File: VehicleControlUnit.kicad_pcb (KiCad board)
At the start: 2 copper layers, 86.6 x 100 mm, 105 parts, among them Con1 LED, Con2 LED, J1 Conn_01x02, J10 USB_C_Receptacle_USB2.0_16P, J11 UART_Breakout, J12 Conn_01x04, J13 Conn_01x04, J14 Conn_01x04, J15 Conn_01x08, J16 Conn_01x08, J2 Precharge_Ready, J4 Conn_01x02, J5 Conn_01x02, J6 Conn_01x04, J7 Conn_01x04, J8 MOTOR_CAN_Breakout, J9 CAR_CAN_Breakout, Q1 PMV35EPER, Q2 IRLML0030, Q3 IRLML0030, SW1 RESET, SW2 BOOT, U1 TLV1117LV33DCYR, U3 ESP32-C6-MINI-1/U, U4 TCMT1106, U5 TCMT1106

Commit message: fuck the rats nest im doing it tomorrow
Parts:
- removed J12, J13: Conn_01x04, utsvt_conn:Molex_MicroFit3.0_1x4xP3.00mm_PolarizingPeg_Vertical
- removed J16: Conn_01x08, Connector_PinHeader_2.54mm:PinHeader_1x08_P2.54mm_Vertical
- removed R28, R29, R30: 1k, Resistor_SMD:R_0805_2012Metric
- added C18: 0.1u, Capacitor_SMD:C_0805_2012Metric, F.Cu at (95.3, 60.7)
- added U6: TCMT1106, Package_SO:SOP-4_4.4x2.6mm_P1.27mm, F.Cu at (97.9, 55.1)
- C1: value 1u -> 220n
- C10, C3: value 0.1u -> 10u
- C11: value 10u -> 0.1u
- C12: value 1u -> 10u
- C13, C15, C7: value 0.1u -> 1u
- C14, C4, C8: value 1u -> 0.1u
- C2: value 10u -> 22n
- C9: value 10u -> 1u
- D1: footprint Active-PrechargeLib:BZT52B12QX -> UTSVT_Passives:BZT52B12QX
- D5: footprint tv diode:PRTR5V0U2X -> UTSVT_Passives:PRTR5V0U2X
- D7, D8: footprint Active-PrechargeLib:SODFL4724X108N -> UTSVT_Passives:SODFL4724X108N
- J1: footprint utsvt_conn:Molex_MicroFit3.0_1x2xP3.00mm_PolarizingPeg_Vertical -> UTSVT_Connectors:Molex_MicroFit3.0_1x2xP3.00mm_PolarizingPeg_Vertical
- J10: value USB_C_Receptacle_USB2.0_16P -> Conn_01x04; footprint USBC:GCT_USB4215-03-A_REVA -> UTSVT_Connectors:Molex_MicroFit3.0_1x4xP3.00mm_PolarizingPeg_Vertical
- J11: value UART_Breakout -> Conn_01x04; footprint Connector_PinHeader_2.54mm:PinHeader_1x02_P2.54mm_Vertical -> UTSVT_Connectors:Molex_MicroFit3.0_1x4xP3.00mm_PolarizingPeg_Vertical
- J14: value Conn_01x04 -> SFH11-PBPC-D05-ST-BK; footprint Connector_PinHeader_2.54mm:PinHeader_1x04_P2.54mm_Vertical -> UTSVT_Connectors:CONN_SFH11-xxxC-D05-ST-XX_SUL
- J15: value Conn_01x08 -> SFH11-PBPC-D05-ST-BK; footprint Connector_PinHeader_2.54mm:PinHeader_1x08_P2.54mm_Vertical -> UTSVT_Connectors:CONN_SFH11-xxxC-D05-ST-XX_SUL
- J2: value Precharge_Ready -> Conn_01x02
- J3: value ~ -> Conn_01x02; footprint UTSVT_Special:LeaderSOM -> Connector_Molex:Molex_Nano-Fit_105309-xx02_1x02_P2.50mm_Vertical
- J4: value Conn_01x02 -> ~; footprint Connector_Molex:Molex_Nano-Fit_105309-xx02_1x02_P2.50mm_Vertical -> UTSVT_Special:LeaderSOM
- J5: value Conn_01x02 -> SFH11-PBPC-D05-ST-BK; footprint Connector_Molex:Molex_Nano-Fit_105309-xx02_1x02_P2.50mm_Vertical -> UTSVT_Connectors:CONN_SFH11-xxxC-D05-ST-XX_SUL
- J6: value Conn_01x04 -> SFH11-PBPC-D05-ST-BK; footprint Connector_Molex:Molex_Nano-Fit_105309-xx04_1x04_P2.50mm_Vertical -> UTSVT_Connectors:CONN_SFH11-xxxC-D05-ST-XX_SUL
- J8: value MOTOR_CAN_Breakout -> Conn_01x04; footprint Connector_PinHeader_2.54mm:PinHeader_1x02_P2.54mm_Vertical -> Connector_Molex:Molex_Nano-Fit_105309-xx04_1x04_P2.50mm_Vertical
- J9: value CAR_CAN_Breakout -> USB_C_Receptacle_USB2.0_16P; footprint Connector_PinHeader_2.54mm:PinHeader_1x02_P2.54mm_Vertical -> UTSVT_Connectors:GCT_USB4215-03-A_REVA
- Q1: value PMV35EPER -> PSMN8R5-40MSDX; footprint Package_TO_SOT_SMD:SOT-23-3 -> UTSVT_Power:BUK7M1780EX
- R1: value 49.9k -> 4k
- R10: value 1k -> 5.1k
- R11: value 10k -> 5.1k
- R12, R8: value 1k -> 10k
- R13: value 5.1k -> 100
- R14: value 5.1k -> 1k
- R16, R21: value 100 -> 4k
- R17, R22: value 4k -> 10k
- R18: value 10k -> 100
- R19, R24, R4: value 4k -> 1k
- R2: value 100 -> 1k
- R25, R26, R3: value 10k -> 1k
- U1: value TLV1117LV33DCYR -> LM74501-Q1; footprint Package_TO_SOT_SMD:SOT-223-3_TabPin2 -> Package_TO_SOT_SMD:SOT-23-8
- U2: value ~ -> TLV1117LV33DCYR; footprint LM66200:SOTFL50P160X60-8N -> Package_TO_SOT_SMD:SOT-223-3_TabPin2
- U3: value ESP32-C6-MINI-1/U -> ~; footprint ESP32-C6-MINI-1:ESP32-C6-MINI-1 -> UTSVT_Power:SOTFL50P160X60-8N
- U4: value TCMT1106 -> ESP32-C6-MINI-1/U; footprint Package_SO:SOP-4_4.4x2.6mm_P1.27mm -> UTSVT_Special:ESP32-C6-MINI-1
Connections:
- C1 pad 1: /Precharge_Ready -> Net-(U1-VCap)
- C1 pad 2: GND -> /LV+
- C11 pad 1: /ESP/5V_USB -> /ESP/3V3
- C12 pad 1: GND -> /ESP/5V_USB
- C12 pad 2: /M_Sense -> GND
- C13 pad 1: Net-(J12-Pin_2) -> GND
- C13 pad 2: GND -> /M_Sense
- C14 pad 1: GND -> Net-(J10-Pin_2)
- C14 pad 2: /MPre_Sense -> GND
- C15 pad 1: Net-(J13-Pin_2) -> GND
- C15 pad 2: GND -> /MPre_Sense
- C16 pad 1: /ESP/RESET -> Net-(J11-Pin_2)
- C17 pad 1: /ESP/BOOT -> /ESP/RESET
- C2 pad 1: +24V -> Net-(Q1-G)
- C2 pad 2: GND -> /LV+
- C4 pad 1: 3V3_LSOM -> +24V
- C5 pad 1: /ESP/5V_USB -> 3V3_LSOM
- C6 pad 1: /ESP/3V3_USB -> /ESP/5V_USB
- C7 pad 1: /ESP/3V3 -> /ESP/3V3_USB
- C8 pad 1: /ESP/3V3_USB -> /ESP/3V3
- C9 pad 1: /ESP/3V3 -> /ESP/3V3_USB
- D1 pad 2: Net-(D1-A) -> GND
- J11 pad 1: /ESP_TX -> +24V
- J11 pad 2: /ESP_RX -> Net-(J11-Pin_2)
- J15 pad 1: /ESP/IO5 -> /ESP/IO10
- J15 pad 2: /ESP/IO6 -> /ESP/IO11
- J15 pad 3: /ESP/IO7 -> /ESP/IO12
- J15 pad 4: /ESP/IO8 -> /ESP/IO13
- J15 pad 5: /ESP/IO9 -> /ESP/USB_D+
- J15 pad 6: /ESP/IO10 -> /ESP/USB_D-
- J15 pad 7: /ESP/IO11 -> unconnected-(J15-Pad7)
- J15 pad 8: /ESP/IO12 -> unconnected-(J15-Pad8)
- J2 pad 1: 3V3_LSOM -> GND
- J2 pad 2: Net-(J2-Pin_2) -> /VPrecharge+
- J3 pad 1: 3V3_LSOM -> GND
- J3 pad 2: 3V3_LSOM -> /VPrecharge-
- J4 pad 1: GND -> 3V3_LSOM
- J4 pad 2: /VPrecharge+ -> 3V3_LSOM
- J5 pad 1: GND -> /M_Enable
- J5 pad 2: /VPrecharge- -> /MPre_Enable
- J6 pad 1: /C_CAN_L -> /M_CAN_H
- J6 pad 2: /C_CAN_H -> /M_CAN_L
- J6 pad 3: /C_CAN_L -> /C_CAN_H
- J6 pad 4: /C_CAN_H -> /C_CAN_L
- J7 pad 1: /M_CAN_L -> /C_CAN_L
- J7 pad 2: /M_CAN_H -> /C_CAN_H
- J8 pad 1: /M_CAN_H -> /M_CAN_L
- J8 pad 2: /M_CAN_L -> /M_CAN_H
- Q1 pad 1: Net-(D1-A) -> /LV+
- Q1 pad 2: +24V -> /LV+
- R1 pad 1: GND -> +24V
- R1 pad 2: Net-(D1-A) -> Net-(LVPWR1-A)
- R10 pad 1: /ESP/3V3_USB -> /ESP/CC1
- R10 pad 2: Net-(D3-A) -> GND
- R11 pad 1: Net-(U2-!ON) -> /ESP/CC2
- R12 pad 1: 3V3_LSOM -> /M_Sense
- R12 pad 2: Net-(U2-ST) -> GND
- R13 pad 1: /ESP/CC1 -> /M_Sense
- R13 pad 2: GND -> Net-(R13-Pad2)
- R14 pad 1: /ESP/CC2 -> Net-(J10-Pin_2)
- R14 pad 2: GND -> Net-(R14-Pad2)
- R15 pad 1: /M_Sense -> /M_Enable
- R16 pad 1: /M_Sense -> Net-(Con1-A)
- R16 pad 2: Net-(R16-Pad2) -> +24V
- R17 pad 1: Net-(J12-Pin_2) -> /MPre_Sense
- R17 pad 2: Net-(R17-Pad2) -> GND
- R18 pad 1: /M_Enable -> /MPre_Sense
- R18 pad 2: GND -> Net-(R18-Pad2)
- R19 pad 1: Net-(Con1-A) -> Net-(J11-Pin_2)
- R19 pad 2: +24V -> Net-(R19-Pad2)
- R2 pad 1: Net-(J2-Pin_2) -> /LED1
- R2 pad 2: /Precharge_Ready -> Net-(LED1-A)
- R20 pad 1: /MPre_Sense -> /MPre_Enable
- R21 pad 1: /MPre_Sense -> Net-(Con2-A)
- R21 pad 2: Net-(R21-Pad2) -> +24V
- R22 pad 1: Net-(J13-Pin_2) -> /ESP/Buttons_LEDs_IO/3V3
- R22 pad 2: Net-(R22-Pad2) -> /ESP/RESET
- R23 pad 1: /MPre_Enable -> /ESP/Buttons_LEDs_IO/3V3
- R23 pad 2: GND -> /ESP/BOOT
- R24 pad 1: Net-(Con2-A) -> /ESP/LED1
- R24 pad 2: +24V -> Net-(LV1-A)
- R25 pad 1: /ESP/Buttons_LEDs_IO/3V3 -> /ESP/LED2
- R25 pad 2: /ESP/RESET -> Net-(LV2-A)
- R26 pad 1: /ESP/Buttons_LEDs_IO/3V3 -> /ESP/LED3
- R26 pad 2: /ESP/BOOT -> Net-(LV3-A)
- R27 pad 1: /ESP/LED1 -> /ESP/LED4
- R27 pad 2: Net-(LV1-A) -> Net-(LV4-A)
- R3 pad 1: /Precharge_Ready -> /LED2
- R3 pad 2: GND -> Net-(LED2-A)
- R4 pad 1: +24V -> /LED3
- R4 pad 2: Net-(LVPWR1-A) -> Net-(LED3-A)
- R5 pad 1: /LED1 -> /LED4
- R5 pad 2: Net-(LED1-A) -> Net-(LED4-A)
- R6 pad 1: /LED2 -> /ESP/5V_USB
- R6 pad 2: Net-(LED2-A) -> Net-(D2-A)
- R7 pad 1: /LED3 -> /ESP/3V3_USB
- R7 pad 2: Net-(LED3-A) -> Net-(D3-A)
- R8 pad 1: /LED4 -> Net-(U3-!ON)
- R8 pad 2: Net-(LED4-A) -> GND
- R9 pad 1: /ESP/5V_USB -> 3V3_LSOM
- R9 pad 2: Net-(D2-A) -> Net-(U3-ST)
- SW1 pad 2: /ESP/RESET -> GND
- SW2 pad 2: /ESP/BOOT -> GND
- U1 pad 1: GND -> Net-(Q1-G)
- U1 pad 2: /ESP/3V3_USB -> /LV+
- U1 pad 3: /ESP/5V_USB -> Net-(U1-VCap)
- U2 pad 2: /ESP/3V3 -> /ESP/3V3_USB
- U2 pad 3: 3V3_LSOM -> /ESP/5V_USB
- U3 pad 2: GND -> /ESP/3V3
- U3 pad 3: /ESP/3V3 -> 3V3_LSOM
- U3 pad 4: unconnected-(U3-NC-Pad4) -> Net-(U3-!ON)
- U3 pad 5: /ESP/IO12 -> GND
- U3 pad 6: /ESP/IO11 -> /ESP/3V3_USB
- U3 pad 7: unconnected-(U3-NC-Pad7) -> /ESP/3V3
- U3 pad 8: /ESP/RESET -> Net-(U3-ST)
- U4 pad 1: Net-(R17-Pad2) -> GND
- U4 pad 3: Net-(R16-Pad2) -> /ESP/3V3
- U4 pad 4: 3V3_LSOM -> unconnected-(U4-NC-Pad4)
- U5 pad 1: Net-(R22-Pad2) -> Net-(R14-Pad2)
- U5 pad 3: Net-(R21-Pad2) -> Net-(R13-Pad2)
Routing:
- net +24V: track 0.00 -> 87.4 mm, vias 39 -> 40
- net /ESP_TX: track 80.2 -> 0.00 mm, vias 1 -> 0
- net /VPrecharge-: track 76.8 -> 0.00 mm, vias 1 -> 0
- net /MPre_Enable: track 88.4 -> 165.3 mm, vias 3 -> 4
- net /LED2: track 51.9 -> 0.00 mm, vias 2 -> 0
- net /ESP/5V_USB: track 12.0 -> 64.0 mm, vias 0 -> 2
- net Net-(U3-!ON): track 0.00 -> 51.6 mm, vias 0 -> 2
- net /LED3: track 49.8 -> 0.00 mm, vias 2 -> 0
- net /ESP/3V3_USB: track 20.3 -> 70.1 mm, vias 0 -> 2
- net /LED1: track 49.4 -> 0.00 mm, vias 2 -> 0
- net /ESP/LED1: track 40.1 -> 0.00 mm, vias 2 -> 0
- net /ESP/LED4: track 37.7 -> 77.7 mm, vias 2 -> 4
- net /ESP_RX: track 78.0 -> 47.4 mm, vias 1 -> 0
- net Net-(J11-Pin_2): track 0.00 -> 30.7 mm, vias 0 -> 1
- net (no net): track 0.00 -> 24.4 mm
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
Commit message: routing done
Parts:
- removed M_Pre_Sen_TP1, M_Sen_TP1: TestPoint, UTSVT_Special:TestPoint_HEX_3mmID
- added C19: 0.1u, Capacitor_SMD:C_0805_2012Metric, F.Cu at (136.0, 51.5)
- added G***: LHRs_LOGO, UTSVT_Logos:LHRs_LOGO, F.Cu at (120.0, 96.8)
- G***: moved to B.Cu
- J2, J3: footprint Connector_Molex:Molex_Nano-Fit_105309-xx02_1x02_P2.50mm_Vertical -> UTSVT_Connectors:Molex_Nano-Fit_105309-xx02_1x02_P2.50mm_Vertical
- J7, J8: footprint Connector_Molex:Molex_Nano-Fit_105309-xx04_1x04_P2.50mm_Vertical -> UTSVT_Connectors:Molex_Nano-Fit_105309-xx04_1x04_P2.50mm_Vertical
- J9: footprint UTSVT_Connectors:GCT_USB4215-03-A_REVA -> UTSVT_Connectors:USB_C_Receptacle_GCT_USB4105-xx-A_16P_TopMnt_Horizontal
- moved J9 91.9 mm to (113.0, 125.2), turned to -90 degrees
- moved U4 81.6 mm to (125.6, 138.1), turned to 180 degrees
- moved G*** 74.1 mm to (140.0, 55.0), turned to 180 degrees
- moved J2 73.8 mm to (165.8, 45.3), turned to 90 degrees
- moved R7 69.0 mm to (130.8, 124.3), turned to 0 degrees
- moved J4 68.6 mm to (150.9, 112.3)
- moved R14 67.3 mm to (119.3, 63.0), turned to 0 degrees
- moved J3 67.0 mm to (156.2, 45.4)
- moved C18 66.0 mm to (160.8, 68.7), turned to 180 degrees
- moved U1 63.7 mm to (139.3, 55.5)
- moved R6 61.8 mm to (128.4, 113.0), turned to 180 degrees
- moved C4 61.7 mm to (150.6, 48.8), turned to 90 degrees
- moved J11 60.8 mm to (114.0, 86.0), turned to 90 degrees
- moved C12 58.5 mm to (124.8, 119.0)
- moved R2 58.4 mm to (176.2, 76.8), turned to 90 degrees
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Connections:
- J14 pad 1: /ESP/IO1 -> /ESP/IO4
- J14 pad 2: /ESP/IO2 -> /ESP/IO13
- J14 pad 4: /ESP/IO4 -> unconnected-(J14-Pad4)
- J14 pad 5: /ESP/IO5 -> /ESP/IO2
- J14 pad 6: /ESP/IO6 -> unconnected-(J14-Pad6)
- J14 pad 7: /ESP/IO7 -> /ESP/IO1
- J14 pad 8: /ESP/IO8 -> unconnected-(J14-Pad8)
- J14 pad 9: /ESP/IO9 -> GND
- J15 pad 1: /ESP/IO10 -> /ESP/IO11
- J15 pad 2: /ESP/IO11 -> /ESP/IO12
- J15 pad 3: /ESP/IO12 -> /ESP/IO9
- J15 pad 4: /ESP/IO13 -> /ESP/IO10
- J15 pad 5: /ESP/USB_D+ -> /ESP/IO7
- J15 pad 6: /ESP/USB_D- -> /ESP/IO8
- J15 pad 7: unconnected-(J15-Pad7) -> /ESP/IO5
- J15 pad 8: unconnected-(J15-Pad8) -> /ESP/IO6
- J15 pad 9: unconnected-(J15-Pad9) -> GND
- J5 pad 1: /M_Enable -> 3V3_LSOM
- J5 pad 2: /MPre_Enable -> /M_Enable
- J5 pad 3: /M_Sense -> /MPre_Enable
- J5 pad 4: /MPre_Sense -> /VPrecharge-
- J5 pad 7: /VPrecharge- -> /M_Sense
- J5 pad 8: /Precharge_Ready -> /MPre_Sense
- J5 pad 9: unconnected-(J5-Pad9) -> GND
- J6 pad 5: /ESP_RX -> /ESP_TX
- J6 pad 6: /ESP_TX -> /ESP_RX
- J6 pad 9: unconnected-(J6-Pad9) -> GND
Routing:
- net /ESP_TX: track 0.00 -> 130.6 mm, vias 0 -> 3
- net /MPre_Enable: track 165.3 -> 63.0 mm
- net +24V: track 87.4 -> 3.36 mm, vias 40 -> 46
- net /ESP_RX: track 47.4 -> 131.0 mm, vias 0 -> 5
- net /Precharge_Ready: track 78.5 -> 0.00 mm, vias 2 -> 0
- net /VPrecharge-: track 0.00 -> 74.6 mm, vias 0 -> 2
- net /LED2: track 0.00 -> 51.9 mm, vias 0 -> 2
- net /ESP/5V_USB: track 64.0 -> 12.6 mm, vias 2 -> 0
- net /LED3: track 0.00 -> 49.8 mm, vias 0 -> 2
- net /ESP/3V3_USB: track 70.1 -> 20.4 mm, vias 2 -> 0
- net /LED1: track 0.00 -> 49.4 mm, vias 0 -> 2
- net Net-(U3-!ON): track 51.6 -> 3.07 mm, vias 2 -> 0
- net 3V3_LSOM: track 153.8 -> 105.7 mm, vias 8 -> 4
- net /ESP/LED1: track 0.00 -> 40.1 mm, vias 0 -> 2
- net /ESP/LED4: track 77.7 -> 37.7 mm, vias 4 -> 2
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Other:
- outline, holes or cut-outs redrawn
- board text added: "24V"
- board text added: "BPS"
- board text added: "Boot"
- board text added: "GND"
- board text added: "Precharge"
- board text added: "Reset"
- board text added: "Sense"
- board text added: "Timeout"
- board text removed: "C_CAN_H C_CAN_L"
- board text removed: "ESP LEDS"
- board text removed: "LSOM LEDS"
- board text removed: "MPre_Sense"
- board text removed: "M_CAN_H M_CAN_L"
- board text removed: "M_Sense"
- board text removed: "TX RX"
- board text removed: "UART_BREAKOUT"

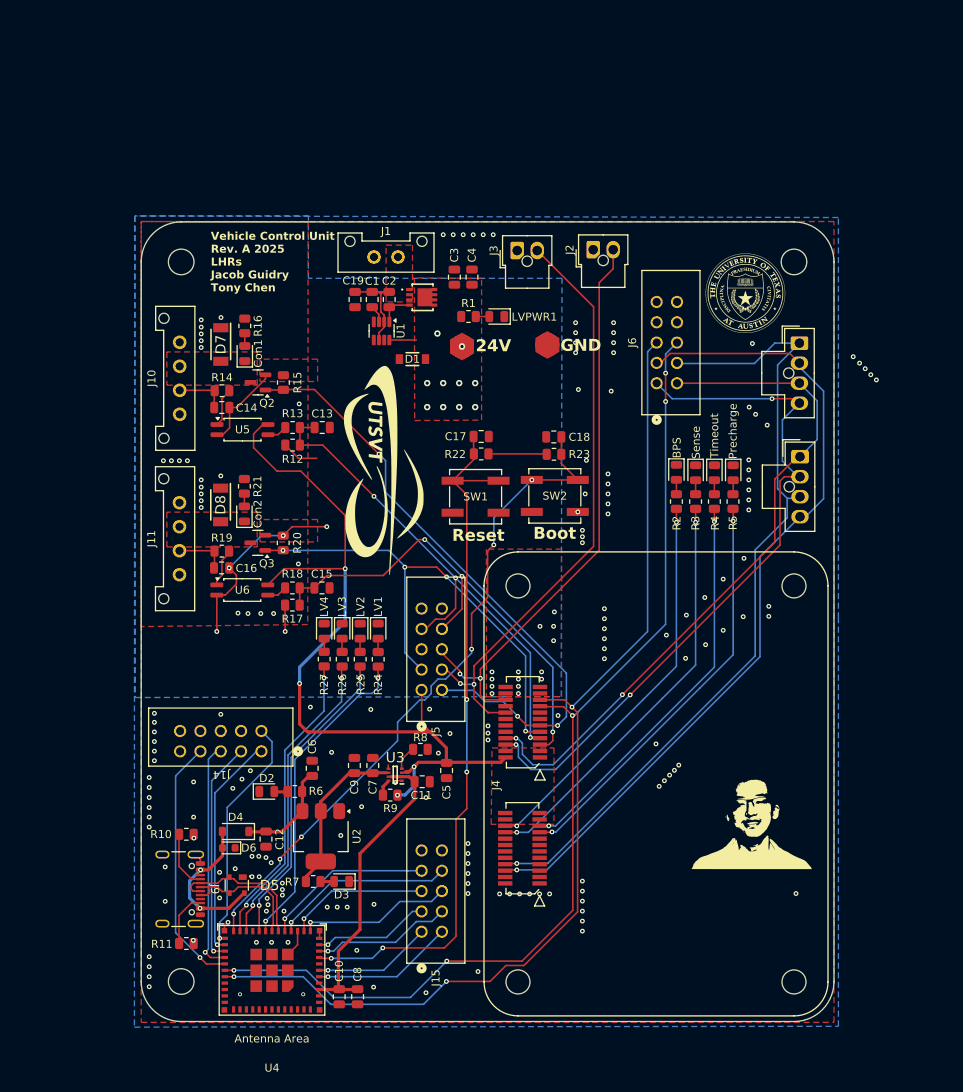
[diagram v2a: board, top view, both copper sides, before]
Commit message: replace microfit with nanofit and some layout adjustments
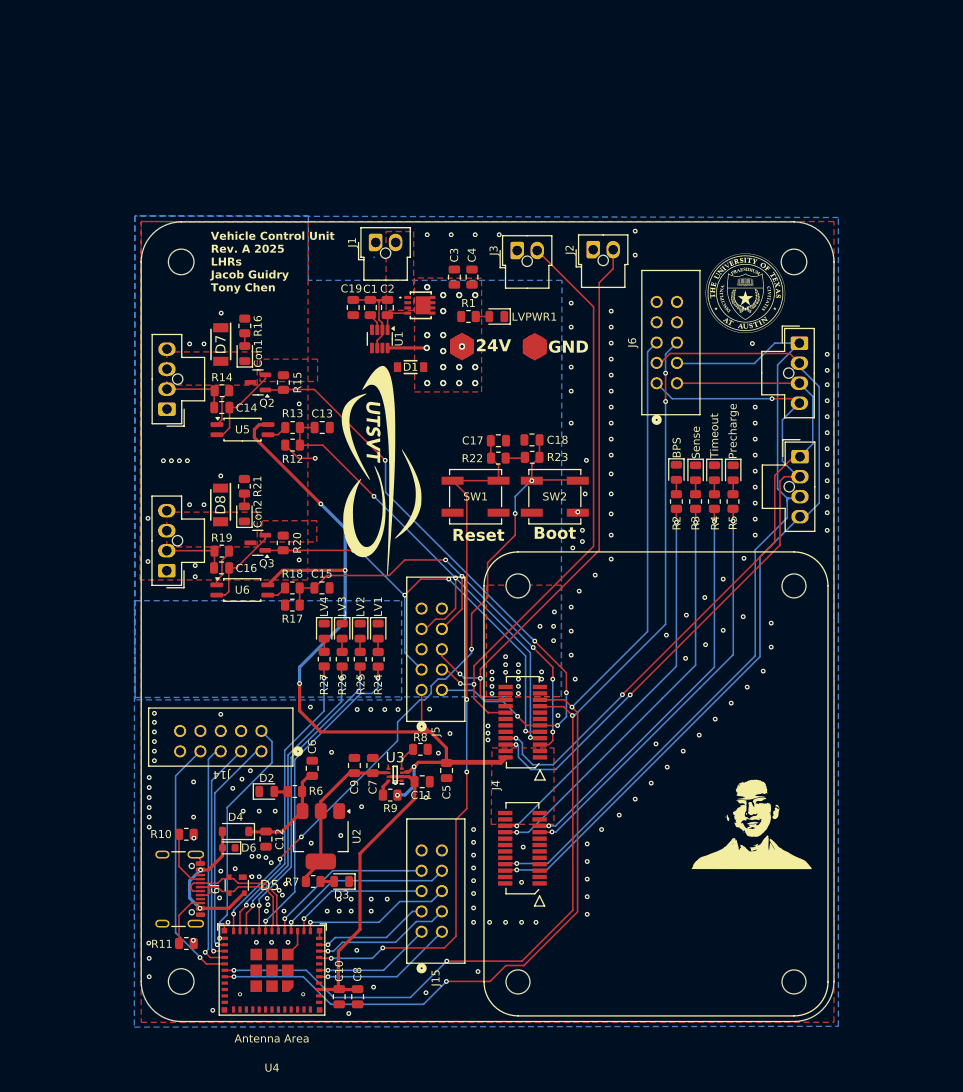
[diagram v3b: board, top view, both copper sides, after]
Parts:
- added G***: LOGO, UTSVT_Logos:Hallock_Image_Tiny, B.Cu at (185.6, 117.2)
- J1: footprint UTSVT_Connectors:Molex_MicroFit3.0_1x2xP3.00mm_PolarizingPeg_Vertical -> UTSVT_Connectors:Molex_Nano-Fit_105309-xx02_1x02_P2.50mm_Vertical
- J10, J11: footprint UTSVT_Connectors:Molex_MicroFit3.0_1x4xP3.00mm_PolarizingPeg_Vertical -> UTSVT_Connectors:Molex_Nano-Fit_105309-xx04_1x04_P2.50mm_Vertical
- moved J10 3.95 mm to (112.7, 62.2), turned to 180 degrees
- moved J11 3.81 mm to (112.7, 82.4), turned to 180 degrees
- moved C18 2.75 mm to (158.1, 69.1)
- moved R23 2.75 mm to (158.1, 71.3)
- moved C17 2.21 mm to (153.9, 69.2)
- moved R22 2.21 mm to (153.9, 71.4)
- moved J1 1.83 mm to (138.6, 44.4), turned to 90 degrees
- moved LVGND_TP1 1.59 mm to (158.4, 57.5)
- moved Q1 1.03 mm to (144.2, 52.3)
- moved U1 1.03 mm to (139.1, 56.5)
- moved C1 1.02 mm to (137.9, 52.5)
- moved C19 1.02 mm to (135.8, 52.5)
- moved C2 1.02 mm to (140.0, 52.5)
- moved D1 1.02 mm to (142.9, 60.0)
- moved G*** 0.27 mm to (139.2, 73.1)
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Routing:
- net GND: track 52.1 -> 35.7 mm, vias 159 -> 183
- net /ESP/Buttons_LEDs_IO/3V3: track 7.30 -> 2.44 mm
- net 3V3_LSOM: track 105.7 -> 103.1 mm, vias 4 -> 5
- net /LV+: track 12.4 -> 10.1 mm
- net /MPre_Sense: track 61.5 -> 59.4 mm, vias 3 -> 5
- net /MPre_Enable: track 63.0 -> 61.1 mm
- net Net-(J11-Pin_2): track 6.52 -> 8.11 mm
- net +24V: track 3.36 -> 4.91 mm, vias 46 -> 51
- net /ESP/RESET: track 88.9 -> 87.7 mm
- net Net-(J10-Pin_2): track 7.16 -> 8.30 mm
- net /ESP/BOOT: track 84.7 -> 84.0 mm
- net /M_Enable: vias 3 -> 5

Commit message: lakshay nitpicks
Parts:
- removed the G*** at (185.6, 117.2)
- removed J14, J15: SFH11-PBPC-D05-ST-BK, UTSVT_Connectors:CONN_SFH11-xxxC-D05-ST-XX_SUL
- added J12: SFH11-PBPC-D05-ST-BK, UTSVT_Connectors:CONN_SFH11-xxxC-D05-ST-XX_SUL, F.Cu at (124.3, 108.0)
- added J13: SFH11-PBPC-D05-ST-BK, UTSVT_Connectors:CONN_SFH11-xxxC-D05-ST-XX_SUL, F.Cu at (144.2, 130.5)
- C10: value 10u -> 1u
- C11: value 0.1u -> 10u
- C12: value 10u -> 0.1u
- C13: value 1u -> 10u
- C14, C16, C8: value 0.1u -> 1u
- C15, C5, C9: value 1u -> 0.1u
- J6: value SFH11-PBPC-D05-ST-BK -> Conn_01x04; footprint UTSVT_Connectors:CONN_SFH11-xxxC-D05-ST-XX_SUL -> UTSVT_Connectors:Molex_Nano-Fit_105309-xx04_1x04_P2.50mm_Vertical
- J8: footprint UTSVT_Connectors:Molex_Nano-Fit_105309-xx04_1x04_P2.50mm_Vertical -> Connector_PinHeader_2.54mm:PinHeader_1x04_P2.54mm_Vertical
- moved C5 57.5 mm to (135.7, 54.1)
- moved C13 42.6 mm to (130.6, 110.1), turned to 90 degrees
- moved C17 38.0 mm to (119.5, 85.3)
- moved C10 29.2 mm to (138.2, 109.8), turned to 90 degrees
- moved C8 28.9 mm to (135.9, 109.8), turned to 90 degrees
- moved C9 28.9 mm to (136.3, 138.7), turned to -90 degrees
- moved C19 27.9 mm to (158.1, 69.2), turned to 180 degrees
- moved C15 25.6 mm to (119.5, 65.2), turned to 0 degrees
- moved J8 24.7 mm to (173.7, 57.0)
- moved C12 21.7 mm to (134.0, 138.7)
- moved J6 21.6 mm to (191.4, 74.3), turned to 0 degrees
- moved C6 16.8 mm to (147.4, 110.3), turned to -90 degrees
- moved C7 16.3 mm to (124.8, 119.0), turned to -90 degrees
- moved J5 10.5 mm to (146.8, 90.2), turned to -90 degrees
- moved C16 9.67 mm to (128.9, 86.3), turned to 90 degrees
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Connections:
- net /VPrecharge+ renamed /Batt_Voltage
- C10 pad 1: /ESP/3V3 -> /ESP/3V3_USB
- C12 pad 1: /ESP/5V_USB -> /ESP/3V3
- C13 pad 1: GND -> /ESP/5V_USB
- C13 pad 2: /M_Sense -> GND
- C14 pad 1: Net-(J10-Pin_2) -> GND
- C14 pad 2: GND -> /M_Sense
- C15 pad 1: GND -> Net-(J10-Pin_2)
- C15 pad 2: /MPre_Sense -> GND
- C16 pad 1: Net-(J11-Pin_2) -> GND
- C16 pad 2: GND -> /MPre_Sense
- C17 pad 1: /ESP/RESET -> Net-(J11-Pin_2)
- C18 pad 1: /ESP/BOOT -> /ESP/RESET
- C19 pad 1: /LV+ -> /ESP/BOOT
- C5 pad 1: 3V3_LSOM -> /LV+
- C6 pad 1: /ESP/5V_USB -> 3V3_LSOM
- C7 pad 1: /ESP/3V3_USB -> /ESP/5V_USB
- C8 pad 1: /ESP/3V3 -> /ESP/3V3_USB
- C9 pad 1: /ESP/3V3_USB -> /ESP/3V3
- J3 pad 2: /VPrecharge- -> /Motor_Voltage
- J4 pad 16: /VPrecharge- -> /Motor_Voltage
- J5 pad 1: 3V3_LSOM -> /M_Sense
- J5 pad 2: /M_Enable -> /MPre_Enable
- J5 pad 3: /MPre_Enable -> /MPre_Sense
- J5 pad 4: /VPrecharge- -> /M_Enable
- J5 pad 5: unconnected-(J5-Pad5) -> /Motor_Voltage
- J5 pad 7: /M_Sense -> /ESP_TX
- J5 pad 8: /MPre_Sense -> /ESP_RX
- J6 pad 1: /M_CAN_H -> /M_CAN_L
- J6 pad 2: /M_CAN_L -> /M_CAN_H
- J6 pad 3: /C_CAN_H -> /C_CAN_L
- J6 pad 4: /C_CAN_L -> /C_CAN_H
- J7 pad 1: /C_CAN_L -> /M_CAN_L
- J7 pad 2: /C_CAN_H -> /M_CAN_H
- J7 pad 3: /M_CAN_L -> /C_CAN_L
- J7 pad 4: /M_CAN_H -> /C_CAN_H
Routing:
- net /Motor_Voltage: track 0.00 -> 75.4 mm, vias 0 -> 1
- net /VPrecharge-: track 74.6 -> 0.00 mm, vias 2 -> 0
- net /ESP_TX: track 130.6 -> 94.7 mm, vias 3 -> 4
- net /ESP_RX: track 131.0 -> 97.0 mm, vias 5 -> 4
- net GND: track 35.7 -> 8.89 mm, vias 183 -> 181
- net /M_CAN_L: track 85.8 -> 95.5 mm
- net 3V3_LSOM: track 103.1 -> 95.4 mm, vias 5 -> 4
- net /M_CAN_H: track 88.9 -> 96.5 mm, vias 3 -> 2
- net /C_CAN_H: track 103.2 -> 97.9 mm
- net +24V: track 4.91 -> 0.00 mm, vias 51 -> 42
- net /C_CAN_L: track 103.1 -> 98.8 mm
- net /MPre_Enable: track 61.1 -> 56.8 mm, vias 4 -> 3
- net /Batt_Voltage: track 72.8 -> 76.0 mm, vias 2 -> 1
- net Net-(R18-Pad2): track 2.53 -> 5.24 mm
- net Net-(R13-Pad2): track 2.53 -> 5.06 mm
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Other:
- board text added: "M_L M_H C_L C_H"
